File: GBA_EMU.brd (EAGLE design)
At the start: 130.7 x 72.9 mm, 100 parts, among them J1 USB-MINIB-5PIN, J2 AVR_SPI, SW1 LEFT, SW2 RIGHT, SW3 PWR_SWITCH, U1 MIC7221, U2 MCP1642B-ADJ, U4 LM4875, U5 Mic5365-2.8Y, U7 AZV321, X2 HEADPHONE

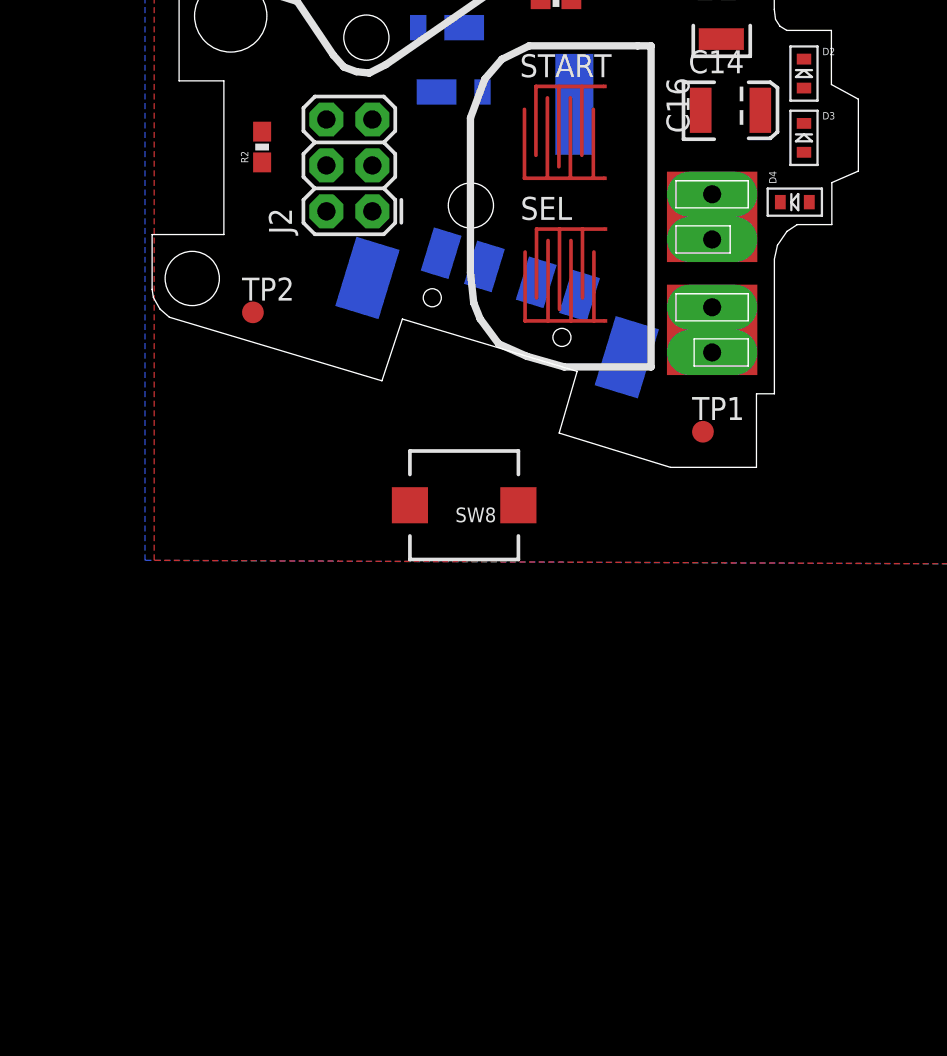
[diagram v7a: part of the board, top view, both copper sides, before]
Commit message: added power down
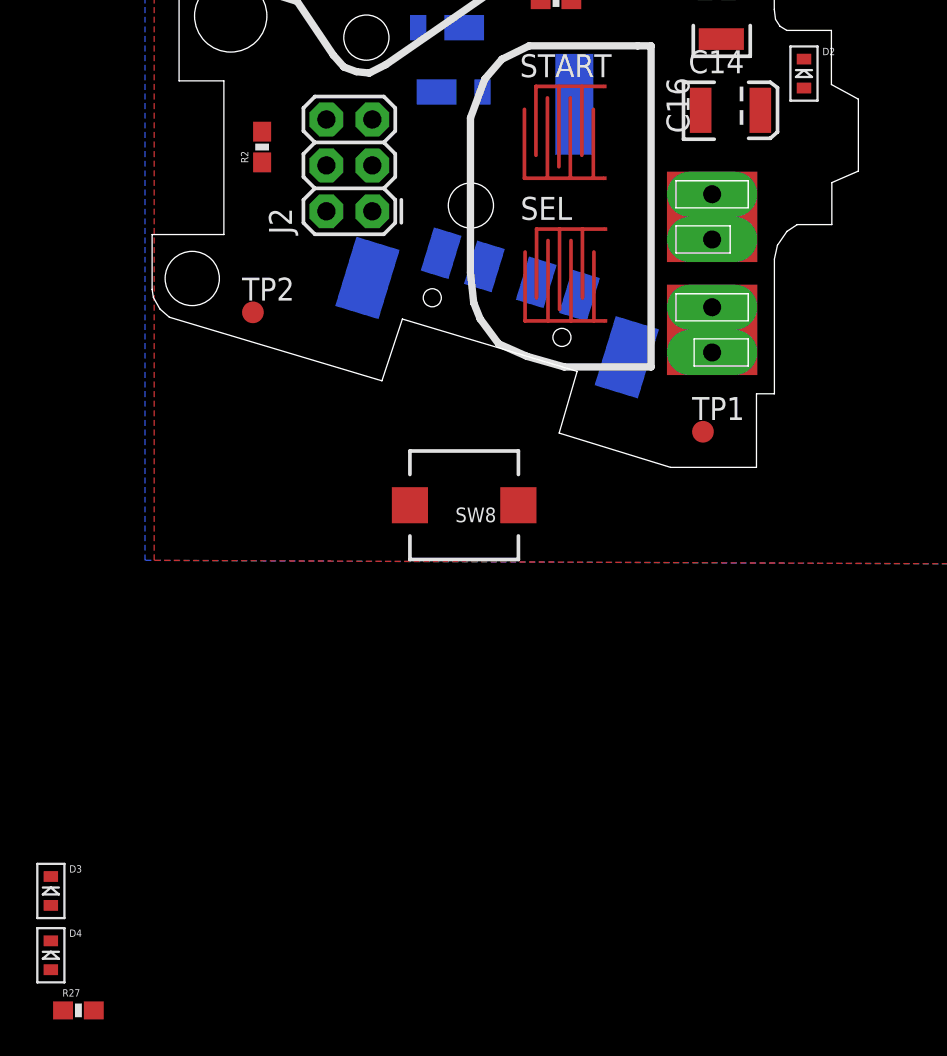
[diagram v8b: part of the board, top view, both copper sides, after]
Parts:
- added R27: 10K, SparkFun-Resistors:0603-RES
- moved D3 58.9 mm to (15.7, -10.7)
- moved D4 58.6 mm to (15.7, -14.2), turned to 0 degrees
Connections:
- removed net N$32: C14.A, L1.P$1, SW8.P$2, U2.8
- new net N$38: COPRO.22, R27.1
- new net PWR_DOWN: C14.A, D4.A, L1.P$1, SW8.P$2, U2.8
- net N$31: now also D4.K; no longer D2.K
- net N$33: now also R27.2; no longer D4.A
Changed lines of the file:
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@@
 <attribute name="PROD_ID" value="RES-07828" x="102.616" y="47.244" size="1.778" layer="27" display="off"/>
 </element>
-<element name="D3" library="adafruit" package="SOD-523" value="" x="57.404" y="30.988"/>
-<element name="D4" library="adafruit" package="SOD-523" value="" x="56.896" y="27.432" rot="R90"/>
 <element name="L1" library="SparkFun-Passives" package="INDUCTOR_4.7UH" value="4.7uH" x="60.96" y="44.196">
 <attribute name="PROD_ID" value="NDUC-10146" x="60.96" y="44.196" size="1.778" layer="27" display="off"/>
@@
 <element name="R24" library="SparkFun-Resistors" package="0603-RES" value="10K" x="49.276" y="45.212">
 <attribute name="PROD_ID" value="RES-00824" x="49.276" y="45.212" size="1.778" layer="27" display="off"/>
+</element>
+<element name="D3" library="adafruit" package="SOD-523" value="" x="15.748" y="-10.668"/>
+<element name="D4" library="adafruit" package="SOD-523" value="" x="15.748" y="-14.224"/>
+<element name="R27" library="SparkFun-Resistors" package="0603-RES" value="10K" x="17.272" y="-17.272">
+<attribute name="PROD_ID" value="RES-00824" x="17.272" y="-17.272" size="1.778" layer="27" display="off"/>
 </element>
 </elements>
@@
 <wire x1="66.566" y1="47.427" x2="122.086" y2="40.64" width="0" layer="19" extent="1-1"/>
 </signal>
-<signal name="N$32">
+<signal name="N$34">
+<contactref element="U2" pad="5"/>
+<contactref element="L1" pad="P$2"/>
+<wire x1="62.46" y1="44.196" x2="62.466" y2="48.727" width="0" layer="19" extent="1-1"/>
+</signal>
+<signal name="N$12">
+<contactref element="D5" pad="2"/>
+<contactref element="D6" pad="2"/>
+<contactref element="SW8" pad="P$1"/>
+<wire x1="37.084" y1="33.528" x2="38.608" y2="37.084" width="0" layer="19" extent="16-16"/>
+<wire x1="35.608" y1="10.668" x2="37.084" y2="33.528" width="0" layer="19" extent="1-16"/>
+</signal>
+<signal name="PI_TFT_DC">
+<contactref element="PCB1" pad="11"/>
+<contactref element="U$1" pad="P$17"/>
+<wire x1="91.844" y1="67.592" x2="114.74" y2="44.16" width="0" layer="19" extent="1-16"/>
+</signal>
+<signal name="UP_BTN">
+<contactref element="PCB1" pad="17"/>
+<contactref element="UP" pad="2"/>
+<wire x1="37.737625" y1="56.34204375" x2="112.94" y2="44.16" width="0" layer="19" extent="1-16"/>
+</signal>
+<signal name="LEFT_BTN">
+<contactref element="LEFT" pad="2"/>
+<contactref element="PCB1" pad="89"/>
+<wire x1="29.69269375" y1="48.213165625" x2="87.74" y2="44.16" width="0" layer="19" extent="1-16"/>
+</signal>
+<signal name="PI_PWM0">
+<contactref element="PCB1" pad="63"/>
+<contactref element="R8" pad="1"/>
+<wire x1="95.54" y1="44.16" x2="136.845" y2="33.655" width="0" layer="19" extent="1-16"/>
+</signal>
+<signal name="COPRO_TX">
+<contactref element="COPRO" pad="9"/>
+</signal>
+<signal name="N$30">
+<contactref element="PCB1" pad="179"/>
+</signal>
+<signal name="N$35">
+<contactref element="PCB1" pad="177"/>
+</signal>
+<signal name="N$36">
+<contactref element="PCB1" pad="199"/>
+<contactref element="PCB1" pad="197"/>
+<wire x1="55.34" y1="44.16" x2="54.74" y2="44.16" width="0" layer="19" extent="16-16"/>
+</signal>
+<signal name="N$37">
+<contactref element="PCB1" pad="200"/>
+<contactref element="PCB1" pad="198"/>
+<wire x1="55.04" y1="52.36" x2="54.44" y2="52.36" width="0" layer="19" extent="16-16"/>
+</signal>
+<signal name="PWR_EN">
+<contactref element="U2" pad="1"/>
+<contactref element="R23" pad="2"/>
+<contactref element="R24" pad="2"/>
+<wire x1="66.566" y1="46.777" x2="103.466" y2="47.244" width="0" layer="19" extent="1-1"/>
+<wire x1="50.126" y1="45.212" x2="66.566" y2="46.777" width="0" layer="19" extent="1-1"/>
+</signal>
+<signal name="PI_SHUTDOWN">
+<contactref element="PCB1" pad="69"/>
+</signal>
+<signal name="N$41">
+<contactref element="PCB1" pad="23"/>
+</signal>
+<signal name="N$42">
+<contactref element="PCB1" pad="27"/>
+</signal>
+<signal name="N$43">
+<contactref element="PCB1" pad="29"/>
+</signal>
+<signal name="N$44">
+<contactref element="COPRO" pad="6"/>
+<contactref element="R24" pad="1"/>
+<wire x1="39.3446" y1="49.092" x2="48.426" y2="45.212" width="0" layer="19" extent="1-16"/>
+</signal>
+<signal name="N$31">
+<contactref element="D3" pad="A"/>
+<contactref element="D4" pad="K"/>
+<wire x1="15.748" y1="-13.424" x2="15.748" y2="-11.468" width="0" layer="19" extent="1-1"/>
+</signal>
+<signal name="N$33">
+<contactref element="D3" pad="K"/>
+<contactref element="R27" pad="2"/>
+<wire x1="18.122" y1="-17.272" x2="15.748" y2="-9.868" width="0" layer="19" extent="1-1"/>
+</signal>
+<signal name="N$38">
+<contactref element="R27" pad="1"/>
+<contactref element="COPRO" pad="22"/>
+<wire x1="16.422" y1="-17.272" x2="30.7594" y2="51.492" width="0" layer="19" extent="1-16"/>
+</signal>
+<signal name="PWR_DOWN">
+<contactref element="D4" pad="A"/>
 <contactref element="U2" pad="8"/>
 <contactref element="C14" pad="A"/>
@@
 <wire x1="52.832" y1="39.75" x2="59.46" y2="44.196" width="0" layer="19" extent="1-1"/>
 <wire x1="41.608" y1="10.668" x2="52.832" y2="39.75" width="0" layer="19" extent="1-1"/>
-</signal>
-<signal name="N$31">
-<contactref element="D2" pad="K"/>
-<contactref element="D3" pad="A"/>
-<wire x1="57.404" y1="30.188" x2="57.404" y2="35.344" width="0" layer="19" extent="1-1"/>
-</signal>
-<signal name="N$33">
-<contactref element="D3" pad="K"/>
-<contactref element="D4" pad="A"/>
-<wire x1="57.696" y1="27.432" x2="57.404" y2="31.788" width="0" layer="19" extent="1-1"/>
-</signal>
-<signal name="N$34">
-<contactref element="U2" pad="5"/>
-<contactref element="L1" pad="P$2"/>
-<wire x1="62.46" y1="44.196" x2="62.466" y2="48.727" width="0" layer="19" extent="1-1"/>
-</signal>
-<signal name="N$12">
-<contactref element="D5" pad="2"/>
-<contactref element="D6" pad="2"/>
-<contactref element="SW8" pad="P$1"/>
-<wire x1="37.084" y1="33.528" x2="38.608" y2="37.084" width="0" layer="19" extent="16-16"/>
-<wire x1="35.608" y1="10.668" x2="37.084" y2="33.528" width="0" layer="19" extent="1-16"/>
-</signal>
-<signal name="PI_TFT_DC">
-<contactref element="PCB1" pad="11"/>
-<contactref element="U$1" pad="P$17"/>
-<wire x1="91.844" y1="67.592" x2="114.74" y2="44.16" width="0" layer="19" extent="1-16"/>
-</signal>
-<signal name="UP_BTN">
-<contactref element="PCB1" pad="17"/>
-<contactref element="UP" pad="2"/>
-<wire x1="37.737625" y1="56.34204375" x2="112.94" y2="44.16" width="0" layer="19" extent="1-16"/>
-</signal>
-<signal name="LEFT_BTN">
-<contactref element="LEFT" pad="2"/>
-<contactref element="PCB1" pad="89"/>
-<wire x1="29.69269375" y1="48.213165625" x2="87.74" y2="44.16" width="0" layer="19" extent="1-16"/>
-</signal>
-<signal name="PI_PWM0">
-<contactref element="PCB1" pad="63"/>
-<contactref element="R8" pad="1"/>
-<wire x1="95.54" y1="44.16" x2="136.845" y2="33.655" width="0" layer="19" extent="1-16"/>
-</signal>
-<signal name="COPRO_TX">
-<contactref element="COPRO" pad="9"/>
-</signal>
-<signal name="N$30">
-<contactref element="PCB1" pad="179"/>
-</signal>
-<signal name="N$35">
-<contactref element="PCB1" pad="177"/>
-</signal>
-<signal name="N$36">
-<contactref element="PCB1" pad="199"/>
-<contactref element="PCB1" pad="197"/>
-<wire x1="55.34" y1="44.16" x2="54.74" y2="44.16" width="0" layer="19" extent="16-16"/>
-</signal>
-<signal name="N$37">
-<contactref element="PCB1" pad="200"/>
-<contactref element="PCB1" pad="198"/>
-<wire x1="55.04" y1="52.36" x2="54.44" y2="52.36" width="0" layer="19" extent="16-16"/>
-</signal>
-<signal name="PWR_EN">
-<contactref element="U2" pad="1"/>
-<contactref element="R23" pad="2"/>
-<contactref element="R24" pad="2"/>
-<wire x1="66.566" y1="46.777" x2="103.466" y2="47.244" width="0" layer="19" extent="1-1"/>
-<wire x1="50.126" y1="45.212" x2="66.566" y2="46.777" width="0" layer="19" extent="1-1"/>
-</signal>
-<signal name="PI_SHUTDOWN">
-<contactref element="PCB1" pad="69"/>
-</signal>
-<signal name="N$41">
-<contactref element="PCB1" pad="23"/>
-</signal>
-<signal name="N$42">
-<contactref element="PCB1" pad="27"/>
-</signal>
-<signal name="N$43">
-<contactref element="PCB1" pad="29"/>
-</signal>
-<signal name="N$44">
-<contactref element="COPRO" pad="6"/>
-<contactref element="R24" pad="1"/>
-<wire x1="39.3446" y1="49.092" x2="48.426" y2="45.212" width="0" layer="19" extent="1-16"/>
+<wire x1="15.748" y1="-15.024" x2="41.608" y2="10.668" width="0" layer="19" extent="1-1"/>
 </signal>
 </signals>
